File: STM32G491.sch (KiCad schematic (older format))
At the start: 32 parts, among them IC1 TPD6E004RSER, J1 Conn_02x10_Odd_Even, J2 Conn_02x10_Odd_Even

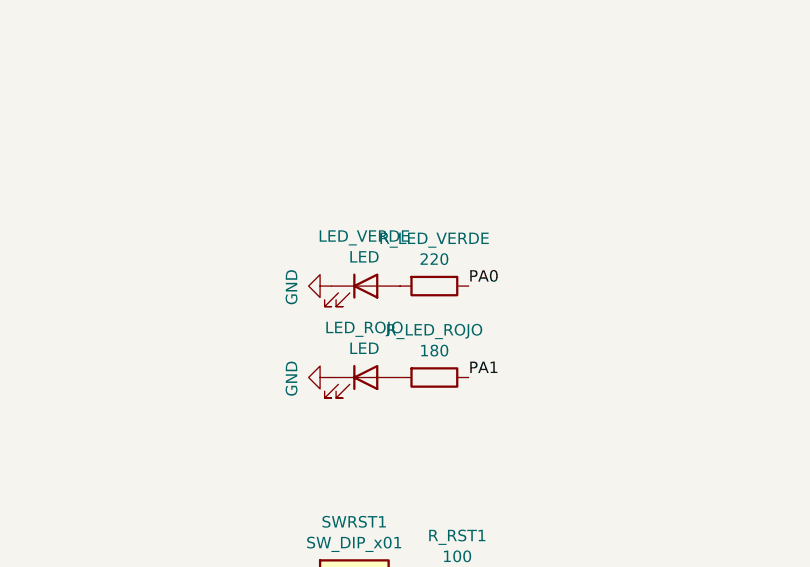
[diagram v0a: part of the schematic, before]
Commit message: Agregar PNGS
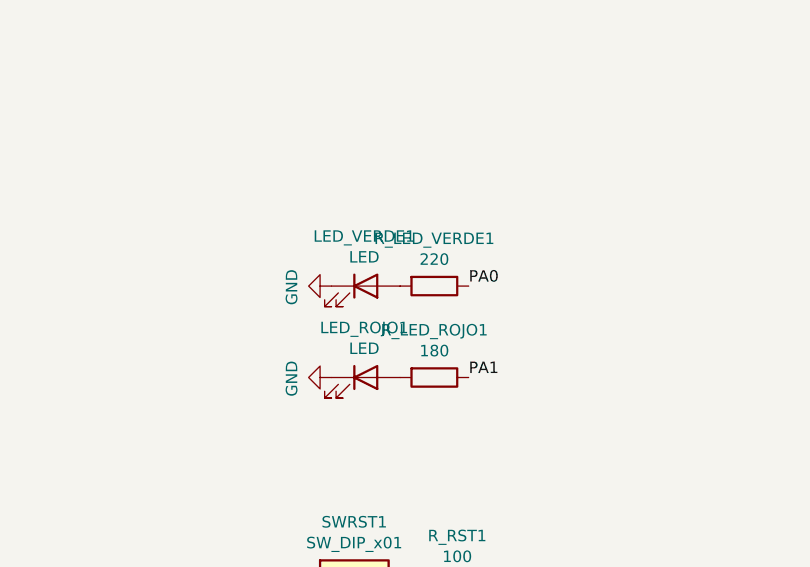
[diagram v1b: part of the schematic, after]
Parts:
- renumbered LED_ROJO to LED_ROJO1, LED_VERDE to LED_VERDE1, R_LED_ROJO to R_LED_ROJO1, R_LED_VERDE to R_LED_VERDE1
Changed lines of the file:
@@
 $EndComp
 $Comp
-L Device:LED LED_VERDE
+L Device:LED LED_VERDE1
 U 1 1 61341CDB
 P 5550 8400
-F 0 "LED_VERDE" H 5543 8617 50  0000 C CNN
+F 0 "LED_VERDE1" H 5543 8617 50  0000 C CNN
 F 1 "LED" H 5543 8526 50  0000 C CNN
 F 2 "LED_SMD:LED_0603_1608Metric" H 5550 8400 50  0001 C CNN
@@
 $EndComp
 $Comp
-L Device:LED LED_ROJO
+L Device:LED LED_ROJO1
 U 1 1 61342A89
 P 5550 8800
-F 0 "LED_ROJO" H 5543 9017 50  0000 C CNN
+F 0 "LED_ROJO1" H 5543 9017 50  0000 C CNN
 F 1 "LED" H 5543 8926 50  0000 C CNN
 F 2 "LED_SMD:LED_0603_1608Metric" H 5550 8800 50  0001 C CNN
@@
 $EndComp
 $Comp
-L Device:R R_LED_VERDE
+L Device:R R_LED_VERDE1
 U 1 1 61342D26
 P 5850 8400
-F 0 "R_LED_VERDE" V 5643 8400 50  0000 C CNN
+F 0 "R_LED_VERDE1" V 5643 8400 50  0000 C CNN
 F 1 "220" V 5734 8400 50  0000 C CNN
 F 2 "Resistor_SMD:R_0402_1005Metric" V 5780 8400 50  0001 C CNN
@@
 $EndComp
 $Comp
-L Device:R R_LED_ROJO
+L Device:R R_LED_ROJO1
 U 1 1 61344170
 P 5850 8800
-F 0 "R_LED_ROJO" V 5643 8800 50  0000 C CNN
+F 0 "R_LED_ROJO1" V 5643 8800 50  0000 C CNN
 F 1 "180" V 5734 8800 50  0000 C CNN
 F 2 "Resistor_SMD:R_0402_1005Metric" V 5780 8800 50  0001 C CNN
